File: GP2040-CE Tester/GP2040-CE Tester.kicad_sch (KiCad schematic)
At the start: 0 parts

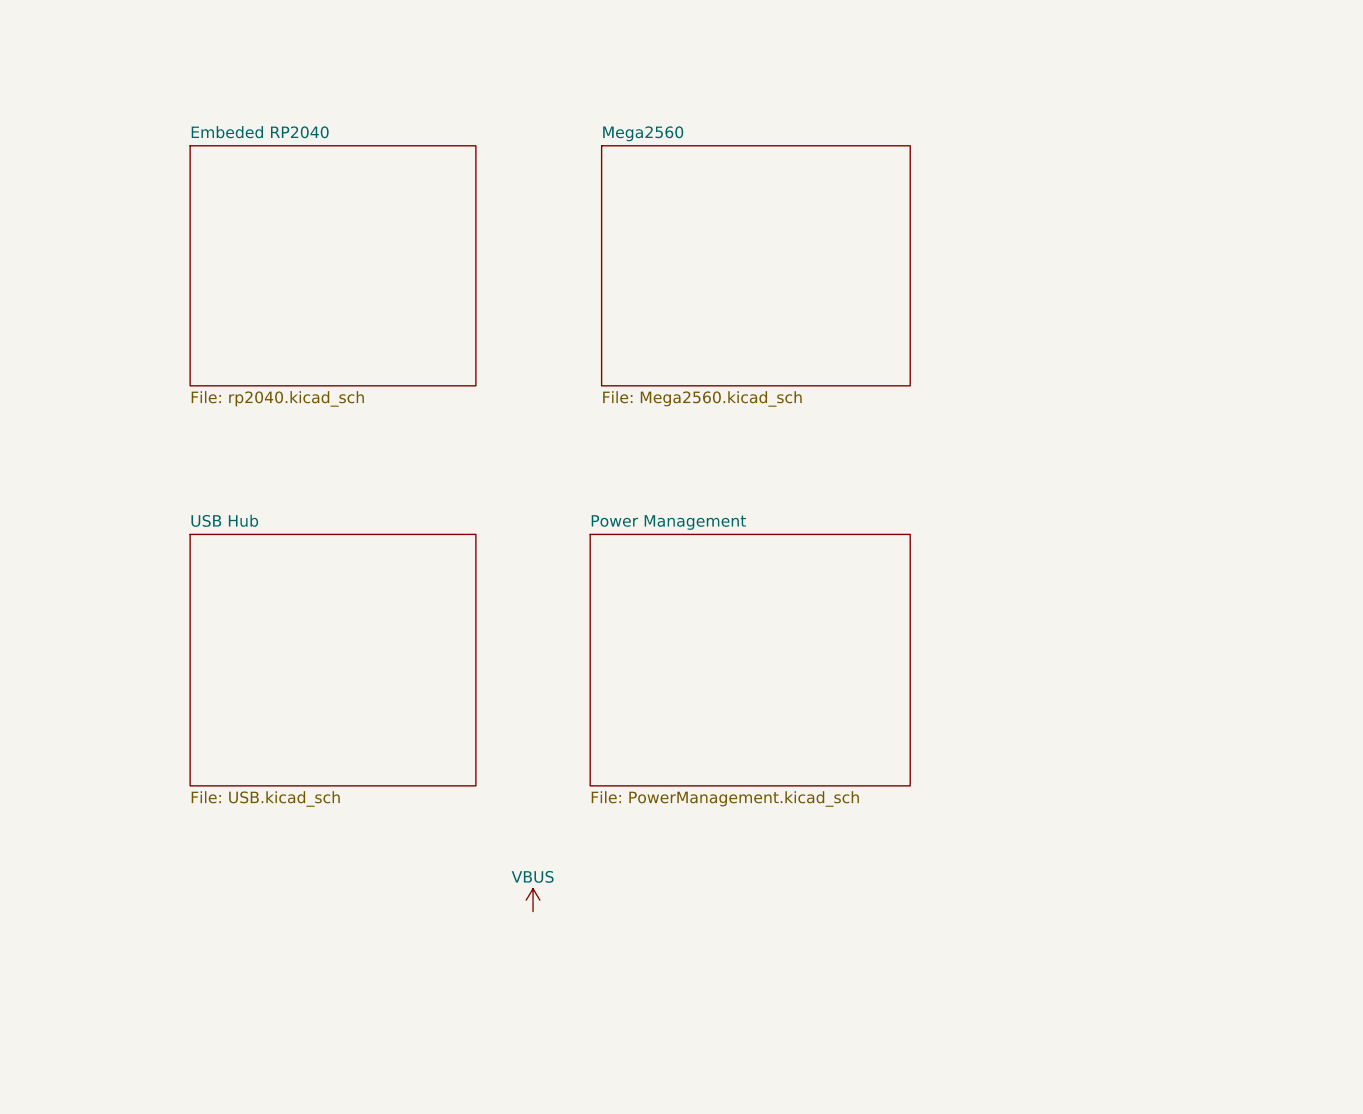
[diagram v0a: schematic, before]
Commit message: adding most of the components, and schematic connections
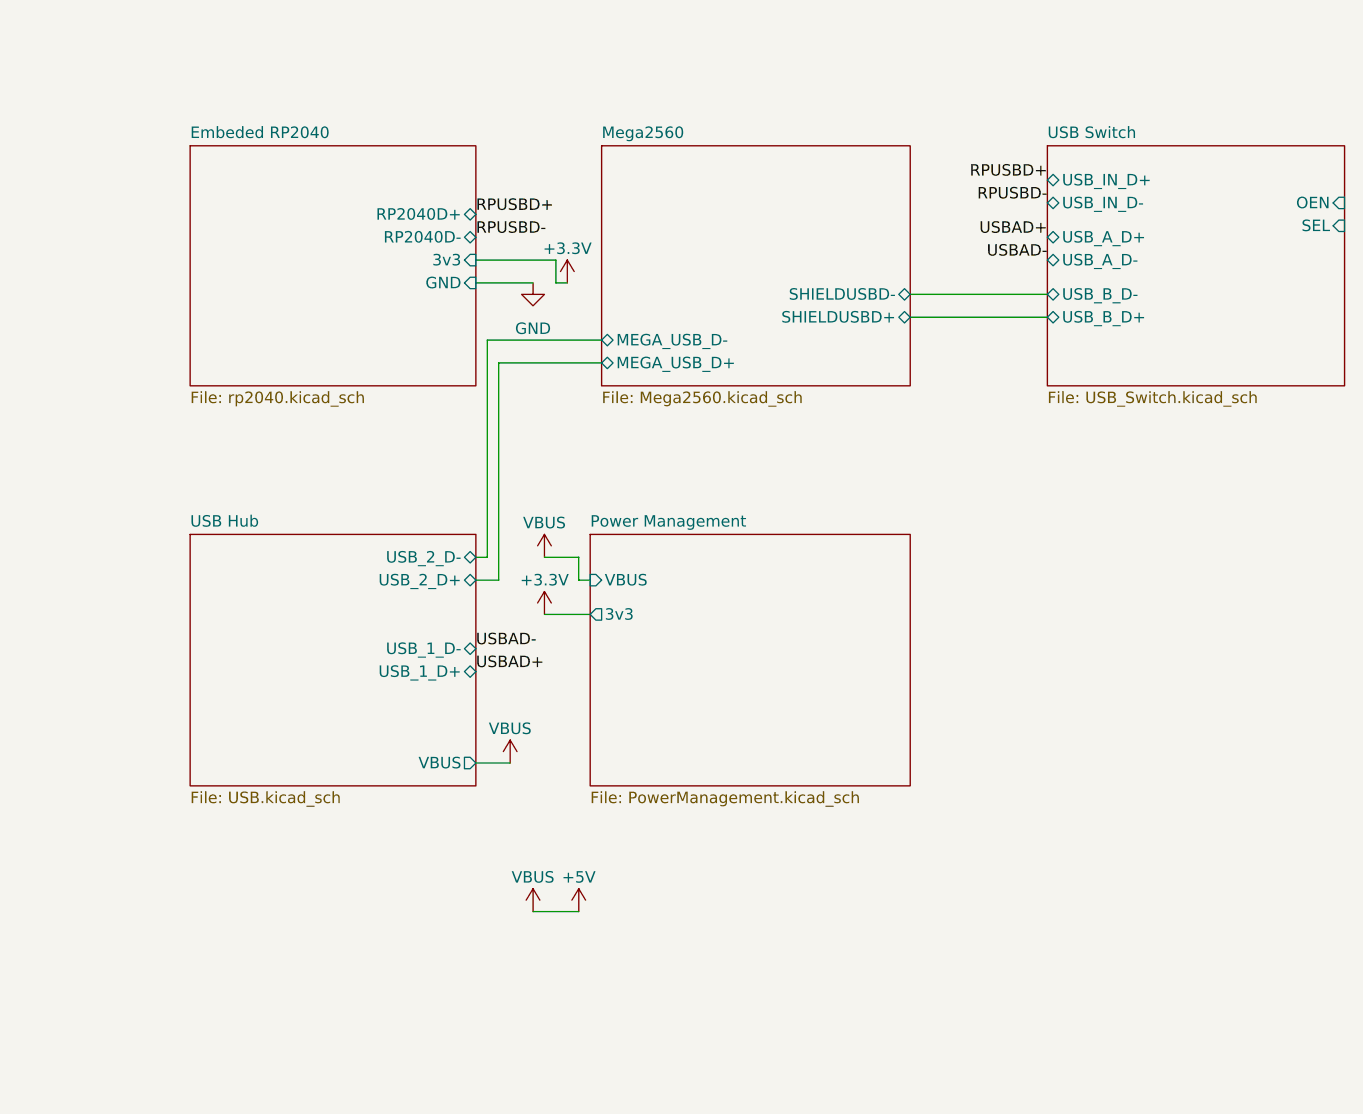
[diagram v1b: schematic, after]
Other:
- added sheet USB Switch (USB_Switch.kicad_sch)
- sheet Embeded RP2040 ports: added 3v3, GND, RP2040D+, RP2040D-; removed none
- sheet Mega2560 ports: added MEGA_USB_D+, MEGA_USB_D-, SHIELDUSBD+, SHIELDUSBD-; removed none
- sheet Power Management ports: added 3v3, VBUS; removed none
- sheet USB Hub ports: added USB_1_D+, USB_1_D-, USB_2_D+, USB_2_D-, VBUS; removed none

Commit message: adding most of the components, and schematic connections
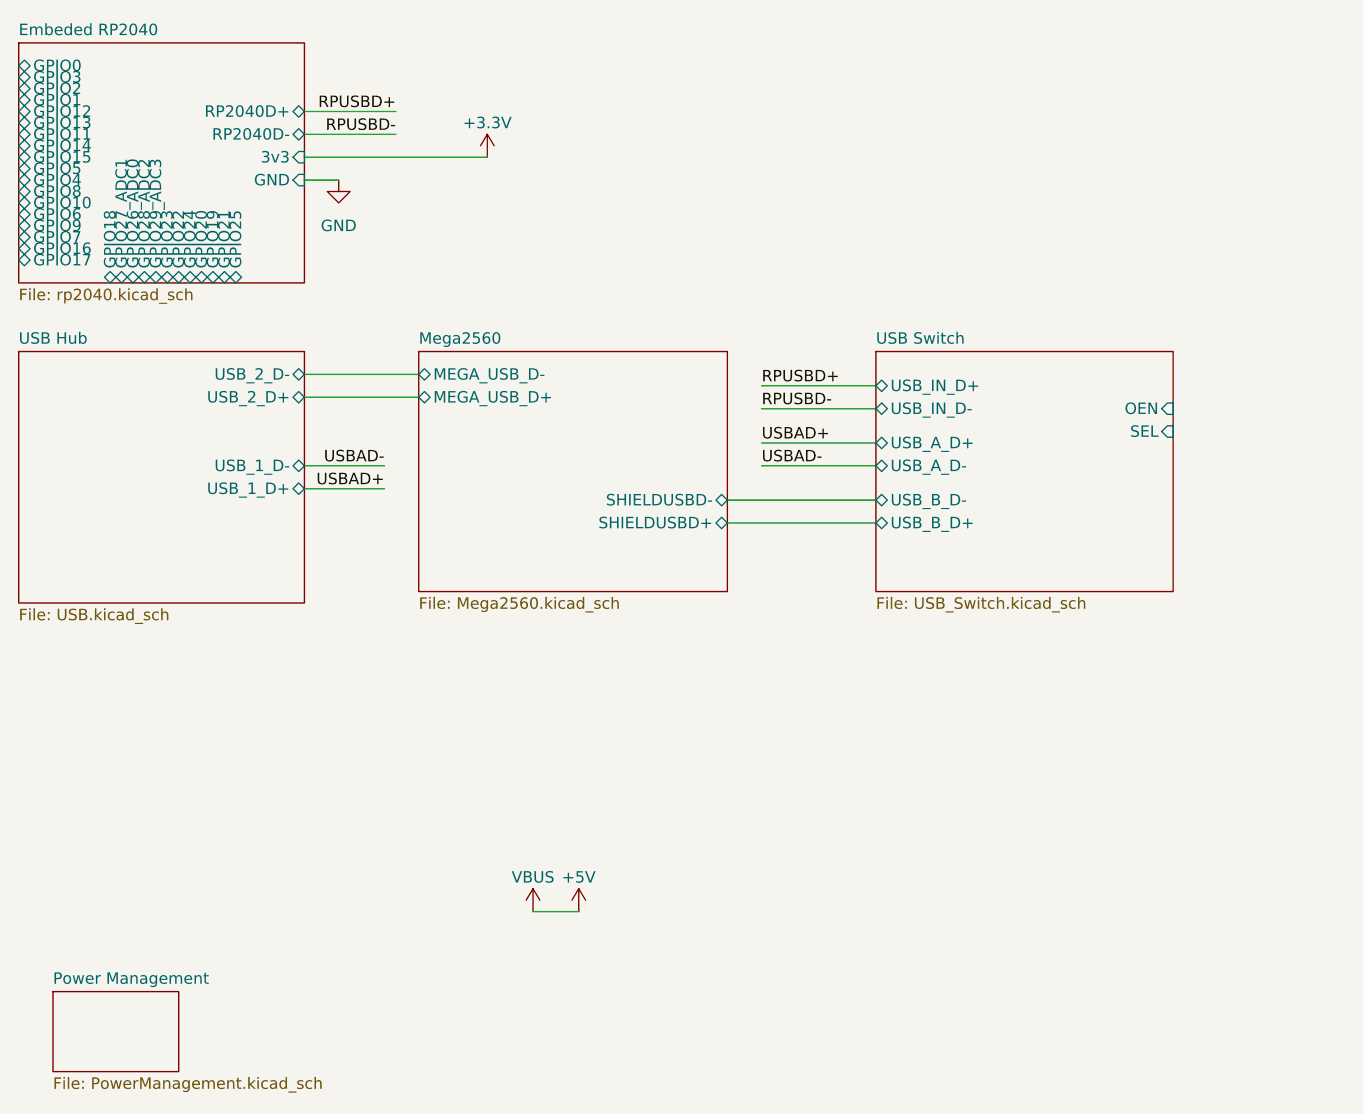
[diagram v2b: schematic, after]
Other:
- sheet Embeded RP2040 ports: added GPIO0, GPIO1, GPIO10, GPIO11, GPIO12, GPIO13, GPIO14, GPIO15, GPIO16, GPIO17, GPIO18, GPIO19, GPIO2, GPIO20, GPIO21, GPIO22, GPIO23, GPIO24, GPIO25, GPIO26_ADC0, GPIO27_ADC1, GPIO28_ADC2, GPIO29_ADC3, GPIO3, GPIO4, GPIO5, GPIO6, GPIO7, GPIO8, GPIO9; removed none
- sheet Power Management ports: added none; removed 3v3, VBUS
- sheet USB Hub ports: added none; removed VBUS
